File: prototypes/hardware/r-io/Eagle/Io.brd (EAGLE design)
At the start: 99.7 x 76.2 mm, 95 parts, among them IC1 AT90CAN128, IC2 MCP2551SO8, IC3 NUP2105L, IC5 LD117ADT50TR, J1 POWER_JACKPTH, Q1 56P2859, Q2 PMV56XN, Q3 PMV56XN, Q4 PMV56XN, Q5 PMV56XN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

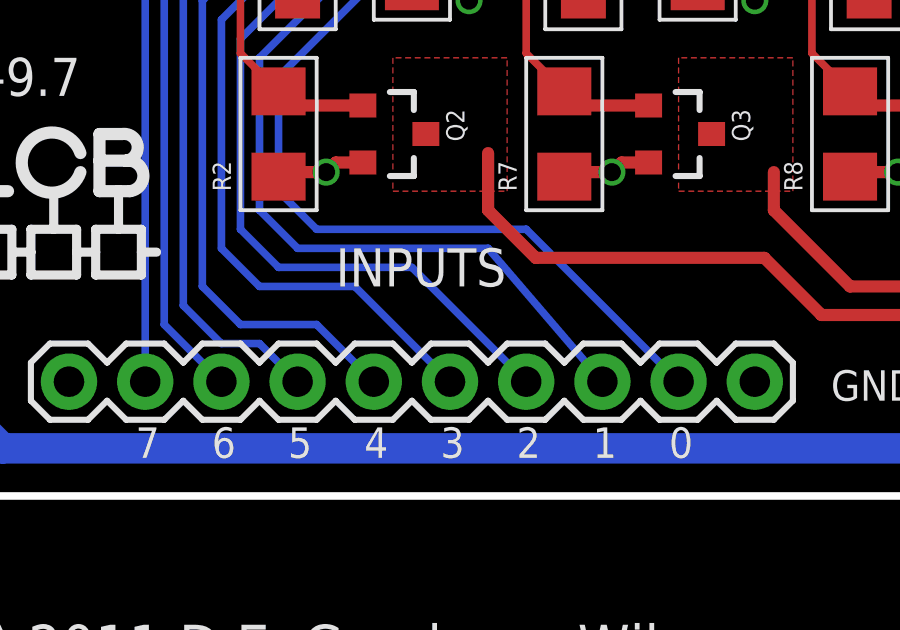
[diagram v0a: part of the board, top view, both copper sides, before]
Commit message: Connected CTS on FTDI header to ground.
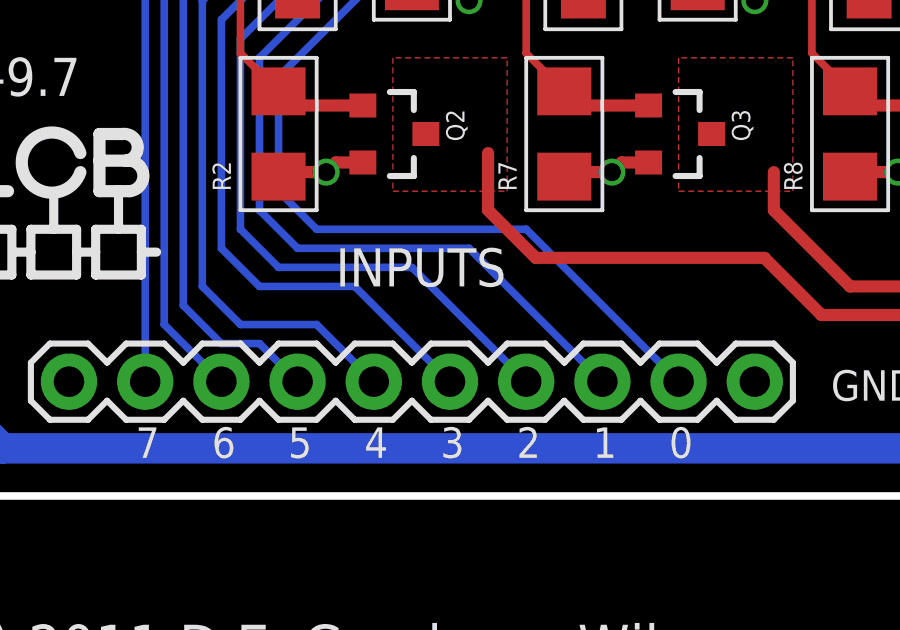
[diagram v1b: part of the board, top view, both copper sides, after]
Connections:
- removed net N$27: JP5.CTS
- net GND: now also JP5.CTS
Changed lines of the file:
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@@
 <param name="mdDrill" value="10mil"/>
 <param name="mdSmdStop" value="0mil"/>
-<param name="msWidth" value="10mil"/>
+<param name="msWidth" value="8mil"/>
 <param name="msDrill" value="12mil"/>
 <param name="msMicroVia" value="12mil"/>
@@
 <vertex x="88.265" y="36.195"/>
 </polygon>
+<contactref element="JP5" pad="CTS"/>
 </signal>
 <signal name="RXCAN">
@@
 <contactref element="IC1" pad="36"/>
 <contactref element="JP3" pad="3"/>
-<wire x1="31.75" y1="3.81" x2="27.94" y2="8.255" width="0.254" layer="16"/>
-<wire x1="27.94" y1="8.255" x2="21.59" y2="8.255" width="0.254" layer="16"/>
+<wire x1="31.75" y1="3.81" x2="27.305" y2="8.255" width="0.254" layer="16"/>
+<wire x1="27.305" y1="8.255" x2="21.59" y2="8.255" width="0.254" layer="16"/>
 <wire x1="21.59" y1="8.255" x2="20.32" y2="9.525" width="0.254" layer="16"/>
 <wire x1="20.32" y1="9.525" x2="20.32" y2="14.605" width="0.254" layer="16"/>
@@
 <wire x1="21.59" y1="69.85" x2="21.59" y2="69.215" width="0.254" layer="1"/>
 </signal>
-<signal name="N$27">
-<contactref element="JP5" pad="CTS"/>
-</signal>
 <signal name="USB_V">

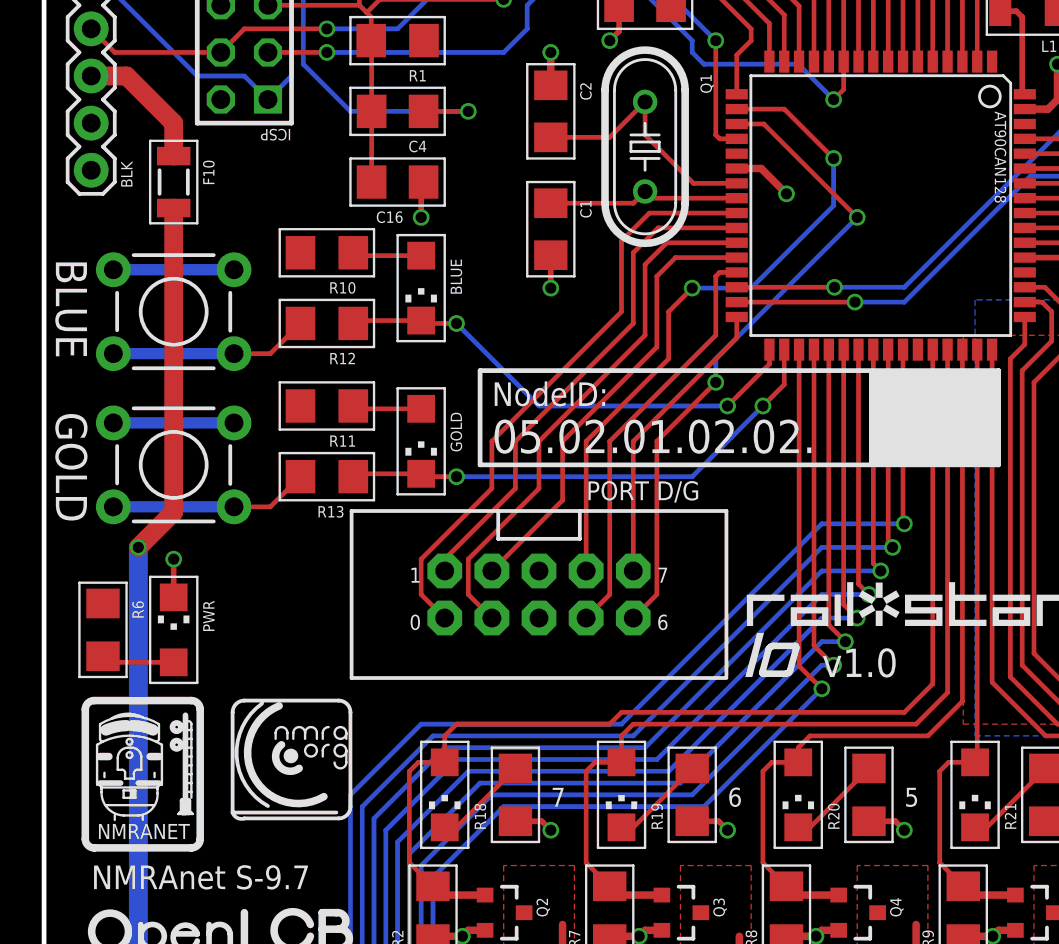
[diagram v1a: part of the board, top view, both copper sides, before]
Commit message: Added default-on solder jumper for CTS line to ground. Added resistor/jumper pair for PG4—the only unused pin—to provide future configuration option.
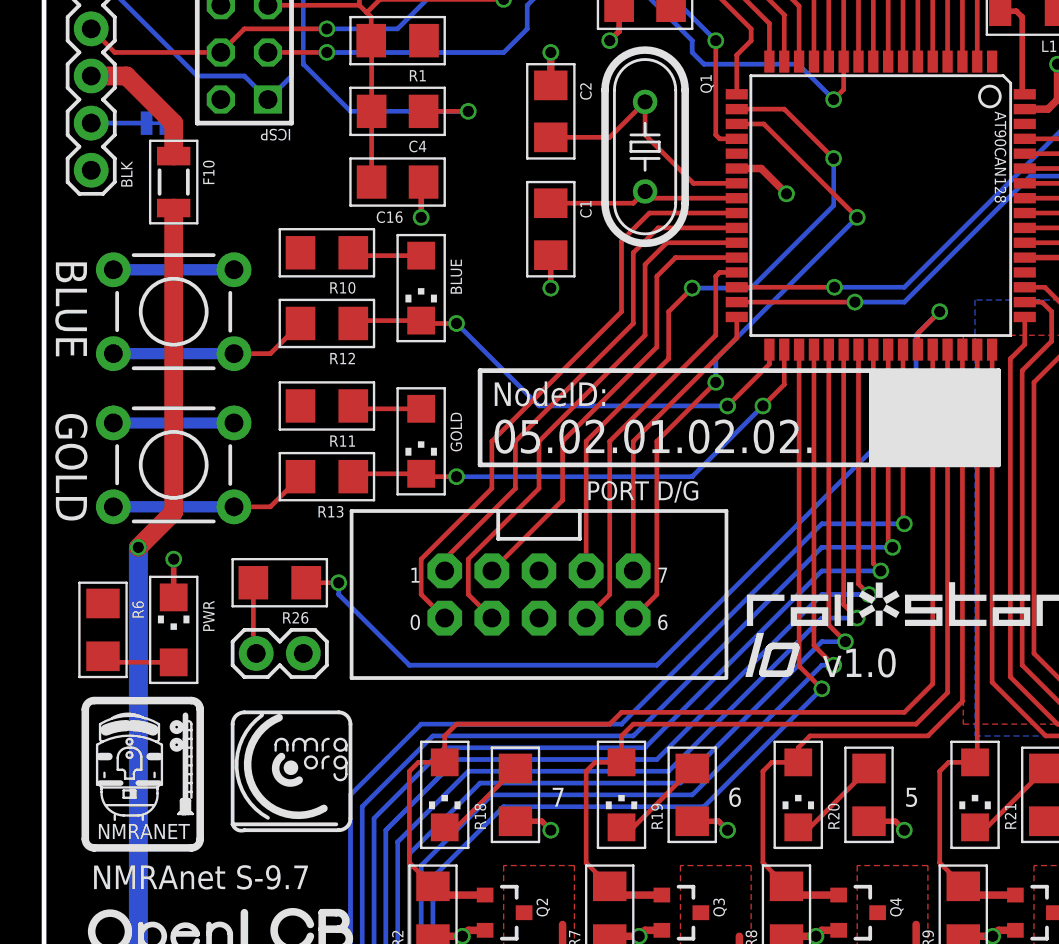
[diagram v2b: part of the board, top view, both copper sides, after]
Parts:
- added JP11: (no value), SparkFun:1X02
- added R26: 100, rcl:R1206
- added SJ1: SOLDERJUMPERTRACE, SparkFun:SJ_2S-TRACE
- moved U$10 0.63 mm to (10.2, 16.5)
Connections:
- new net N$23: JP5.CTS, SJ1.1
- new net N$25: JP11.2, R26.2
- net GND: now also JP11.1, SJ1.2; no longer JP5.CTS
- net PG2: now also R26.1
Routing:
- net PG2: track 0.00 -> 49.0 mm, vias 0 -> 2
- net N$25: track 0.00 -> 3.87 mm
- net N$23: track 0.00 -> 2.98 mm
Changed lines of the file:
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@@
 <wire x1="23.495" y1="41.275" x2="51.435" y2="41.275" width="0.254" layer="21"/>
 <wire x1="51.435" y1="41.275" x2="51.435" y2="36.195" width="0.254" layer="21"/>
+<wire x1="10.16" y1="31.115" x2="15.24" y2="31.115" width="0.127" layer="21"/>
+<wire x1="15.24" y1="31.115" x2="15.24" y2="28.575" width="0.127" layer="21"/>
+<wire x1="15.24" y1="28.575" x2="10.16" y2="28.575" width="0.127" layer="21"/>
+<wire x1="10.16" y1="28.575" x2="10.16" y2="31.115" width="0.127" layer="21"/>
 </plain>
 <attributes>
@@
 </element>
 <element name="U$9" library="OpenLCB" package="OPENLCB_LOGOV" value="" x="1.905" y="6.985"/>
-<element name="U$10" library="OpenLCB" package="NMRA_ORG_SMALL" value="" x="10.16" y="17.145"/>
+<element name="U$10" library="OpenLCB" package="NMRA_ORG_SMALL" value="" x="10.16" y="16.51"/>
 <element name="U$2" library="OpenLCB" package="CURRENT_DRAWV" value="" x="84.455" y="42.2275" rot="MR0"/>
 <element name="U$3" library="OpenLCB" package="CURRENT_PROVIDEV" value="" x="83.5025" y="34.925" rot="MR0"/>
@@
 <element name="U$5" library="Railstars" package="LOGO_IO_V" value="" x="37.7825" y="24.765"/>
 <element name="U$4" library="OpenLCB" package="NMRANET_LOGO_MED" value="" x="1.905" y="15.24"/>
+<element name="SJ1" library="SparkFun" package="SJ_2S-TRACE" value="SOLDERJUMPERTRACE" x="6.0325" y="54.61" rot="MR180"/>
+<element name="R26" library="rcl" package="R1206" value="100" x="12.7" y="29.845" smashed="yes" rot="R180">
+<attribute name="NAME" x="14.2875" y="28.2575" size="0.6096" layer="21" rot="R180"/>
+</element>
+<element name="JP11" library="SparkFun" package="1X02" value="" x="13.97" y="26.035" smashed="yes" rot="R180">
+<attribute name="VALUE" x="15.24" y="29.21" size="1.27" layer="27" rot="R180"/>
+</element>
 </elements>
 <signals>
@@
 <vertex x="88.265" y="36.195"/>
 </polygon>
-<contactref element="JP5" pad="CTS"/>
+<contactref element="SJ1" pad="2"/>
+<contactref element="JP11" pad="1"/>
 </signal>
 <signal name="RXCAN">
@@
 <signal name="PG2">
 <contactref element="IC1" pad="43"/>
+<contactref element="R26" pad="1"/>
+<wire x1="14.122" y1="29.845" x2="15.875" y2="29.845" width="0.254" layer="1"/>
+<via x="15.875" y="29.845" extent="1-16" drill="0.6"/>
+<wire x1="15.875" y1="29.845" x2="15.875" y2="29.21" width="0.254" layer="16"/>
+<wire x1="15.875" y1="29.21" x2="19.685" y2="25.4" width="0.254" layer="16"/>
+<wire x1="19.685" y1="25.4" x2="33.02" y2="25.4" width="0.254" layer="16"/>
+<wire x1="33.02" y1="25.4" x2="46.99" y2="39.37" width="0.254" layer="16"/>
+<wire x1="46.99" y1="39.37" x2="46.99" y2="43.18" width="0.254" layer="16"/>
+<wire x1="46.99" y1="43.18" x2="48.26" y2="44.45" width="0.254" layer="16"/>
+<via x="48.26" y="44.45" extent="1-16" drill="0.6"/>
+<wire x1="48.26" y1="44.45" x2="47.085" y2="43.275" width="0.254" layer="1"/>
+<wire x1="47.085" y1="42.4053" x2="47.085" y2="43.275" width="0.254" layer="1"/>
 </signal>
 <signal name="AREF">
@@
 <wire x1="22.228" y1="16.665" x2="25.4" y2="19.837" width="0.254" layer="1"/>
 </signal>
+<signal name="N$23" class="2">
+<contactref element="JP5" pad="CTS"/>
+<contactref element="SJ1" pad="1"/>
+<wire x1="5.5245" y1="54.61" x2="2.54" y2="54.61" width="0.254" layer="16"/>
+</signal>
+<signal name="N$25">
+<contactref element="R26" pad="2"/>
+<contactref element="JP11" pad="2"/>
+<wire x1="11.278" y1="29.845" x2="11.278" y2="26.187" width="0.254" layer="1"/>
+<wire x1="11.278" y1="26.187" x2="11.43" y2="26.035" width="0.254" layer="1"/>
+</signal>
 </signals>

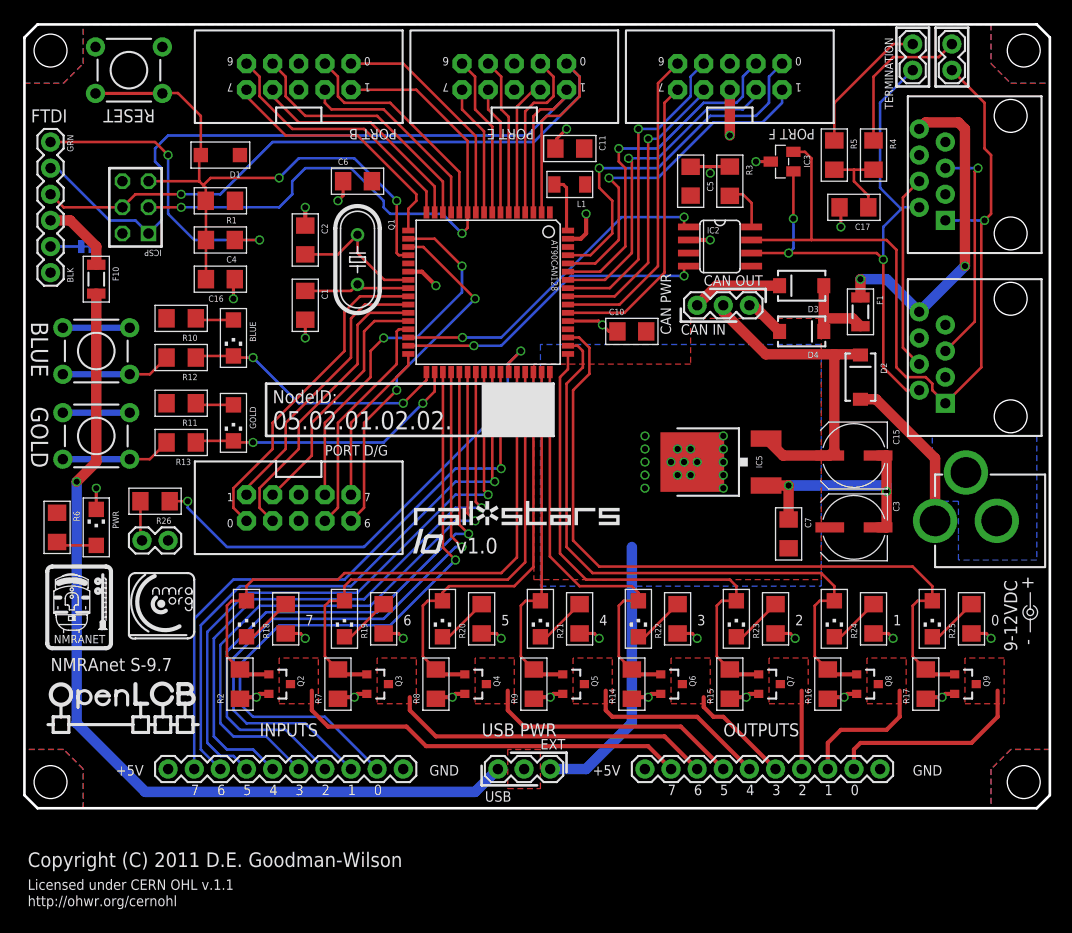
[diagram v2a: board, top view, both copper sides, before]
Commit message: Fattened up the labels.  Rerouted to avoid running under the crystal.  Moved Reset button slightly away from mounting hole.
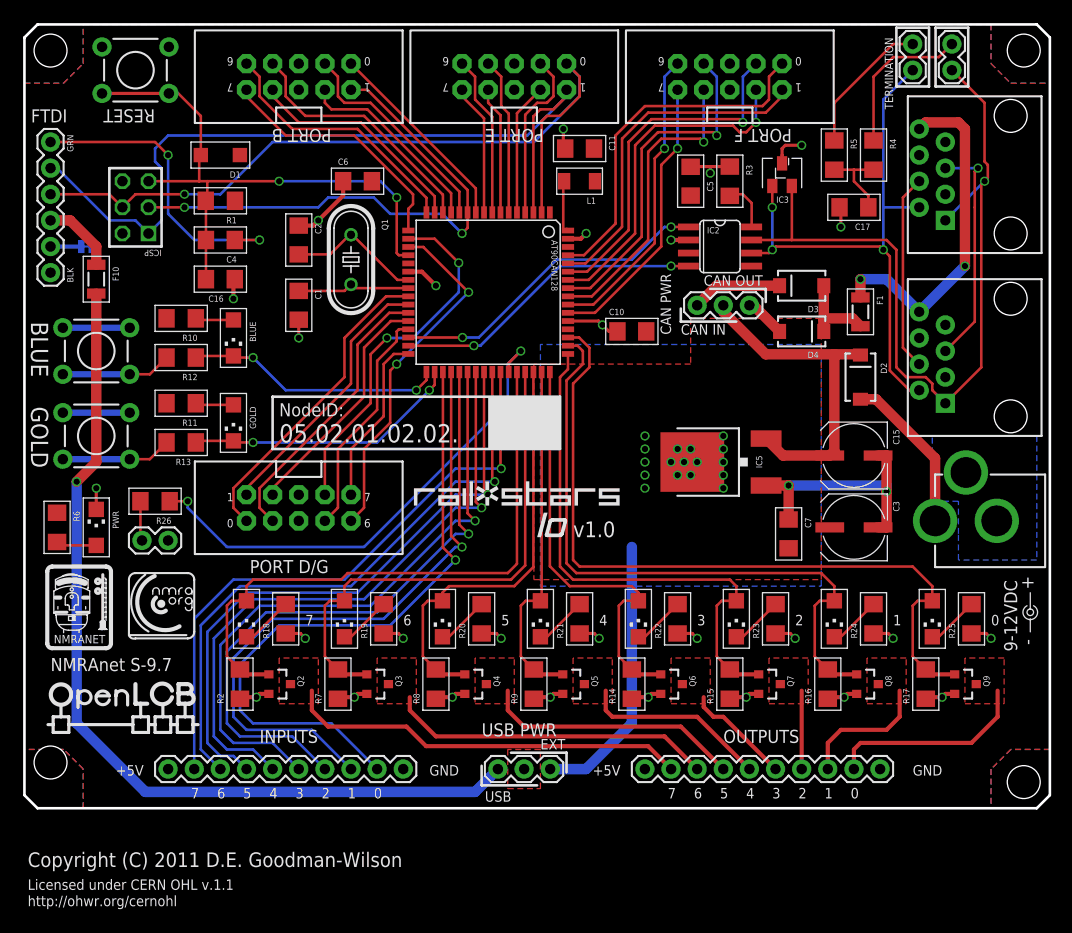
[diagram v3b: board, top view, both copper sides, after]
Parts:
- moved U$5 12.2 mm to (49.8, 26.4)
- moved U$1 1.91 mm to (37.5, 29.2)
- moved IC3 1.27 mm to (73.7, 61.6), turned to 0 degrees
- moved L1 1.00 mm to (54.0, 61.0)
- moved C11 0.95 mm to (54.0, 64.1)
- moved S1 0.63 mm to (10.8, 71.8)
- moved C1 0.63 mm to (26.7, 48.9)
- moved C2 0.63 mm to (26.7, 55.2)
- moved Q1 0.63 mm to (31.8, 53.3)
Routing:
- net PB1: track 58.4 -> 52.1 mm
- net CAN_H: track 82.4 -> 79.2 mm
- net PB0: track 22.5 -> 19.5 mm
- net PF4: track 30.8 -> 33.4 mm
- net GND: track 117.1 -> 115.0 mm, vias 32 -> 30
- net CAN_L: track 59.2 -> 57.2 mm
- net PF7: track 29.3 -> 27.6 mm, vias 0 -> 1
- net PF6: track 30.8 -> 29.3 mm, vias 0 -> 1
- net PD0: track 32.2 -> 30.7 mm
- net RESET: track 60.2 -> 58.7 mm
- net PF5: track 28.8 -> 30.1 mm
- net PD1: track 27.5 -> 26.2 mm
- net PF3: track 32.1 -> 33.3 mm
- net PD2: track 28.9 -> 27.8 mm
- net PA0: track 71.9 -> 73.0 mm
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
